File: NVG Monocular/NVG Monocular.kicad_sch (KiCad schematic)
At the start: 13 parts, among them U1 MP2696AGQ-0000-P

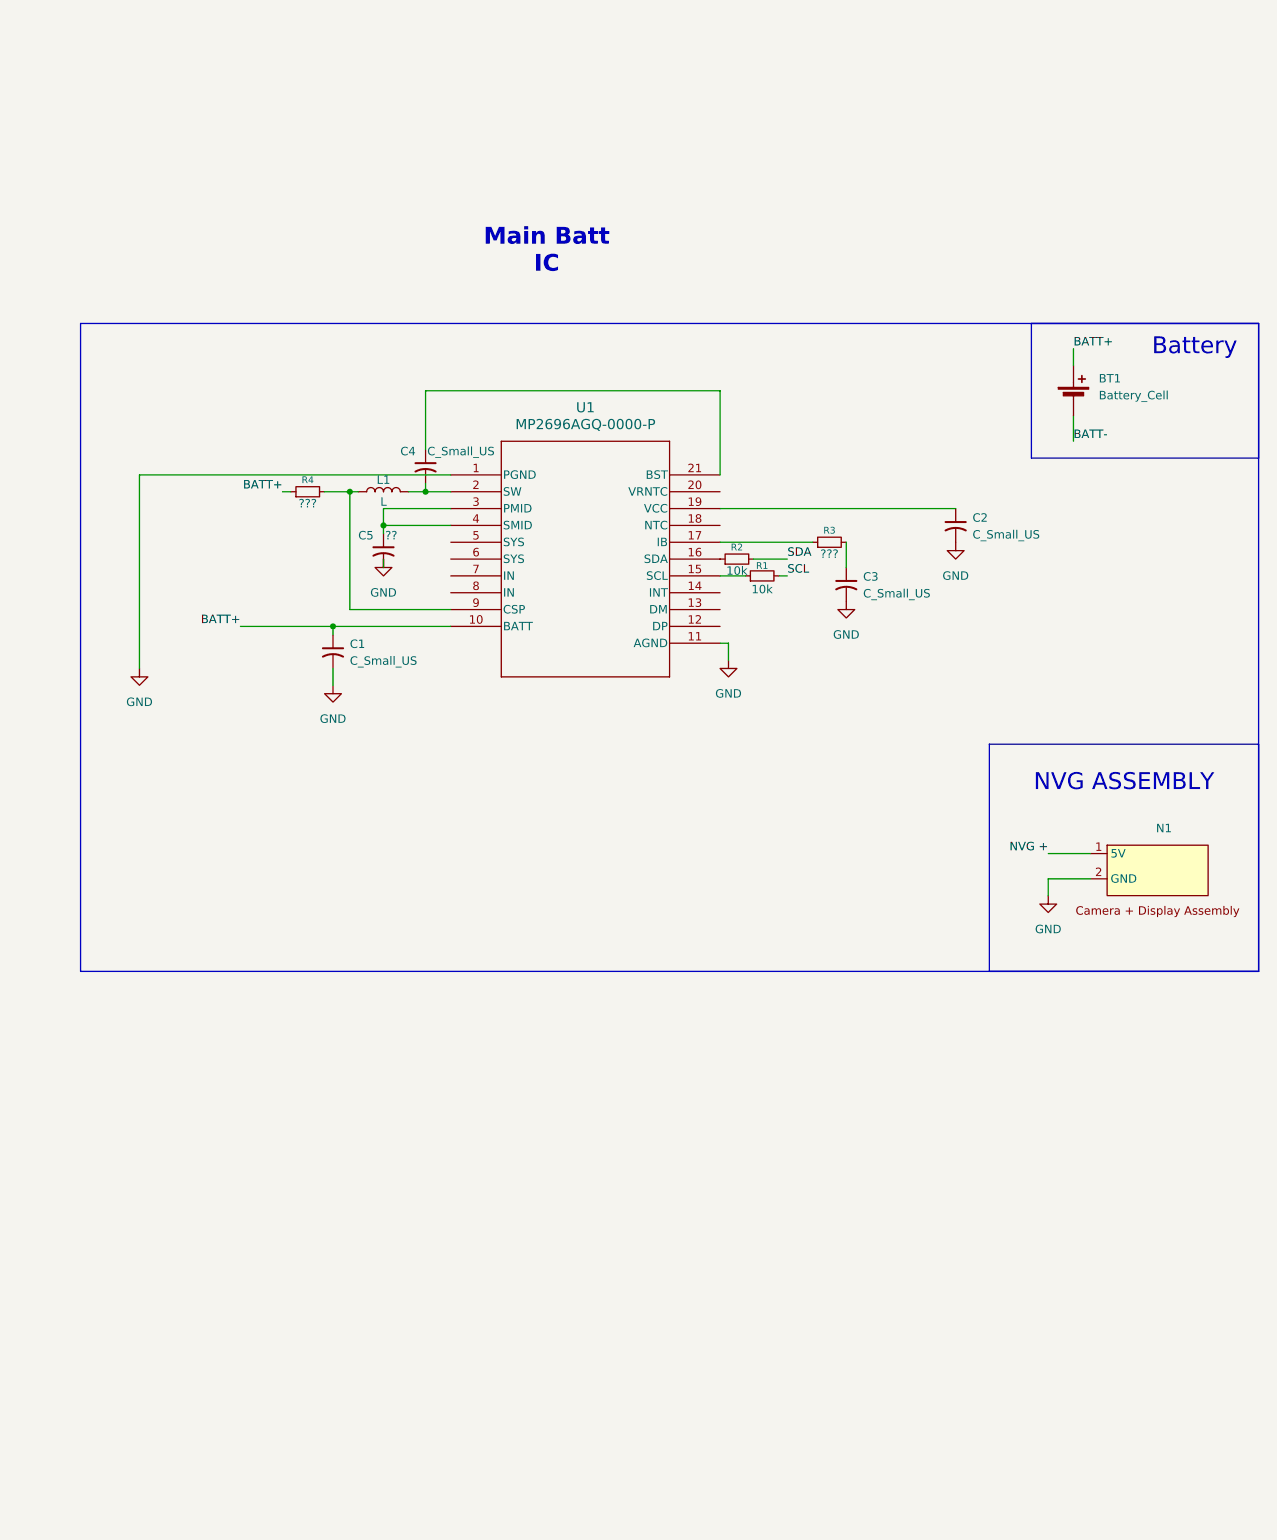
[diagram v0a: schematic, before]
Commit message: Added USB-C and speced out Charge IC passives
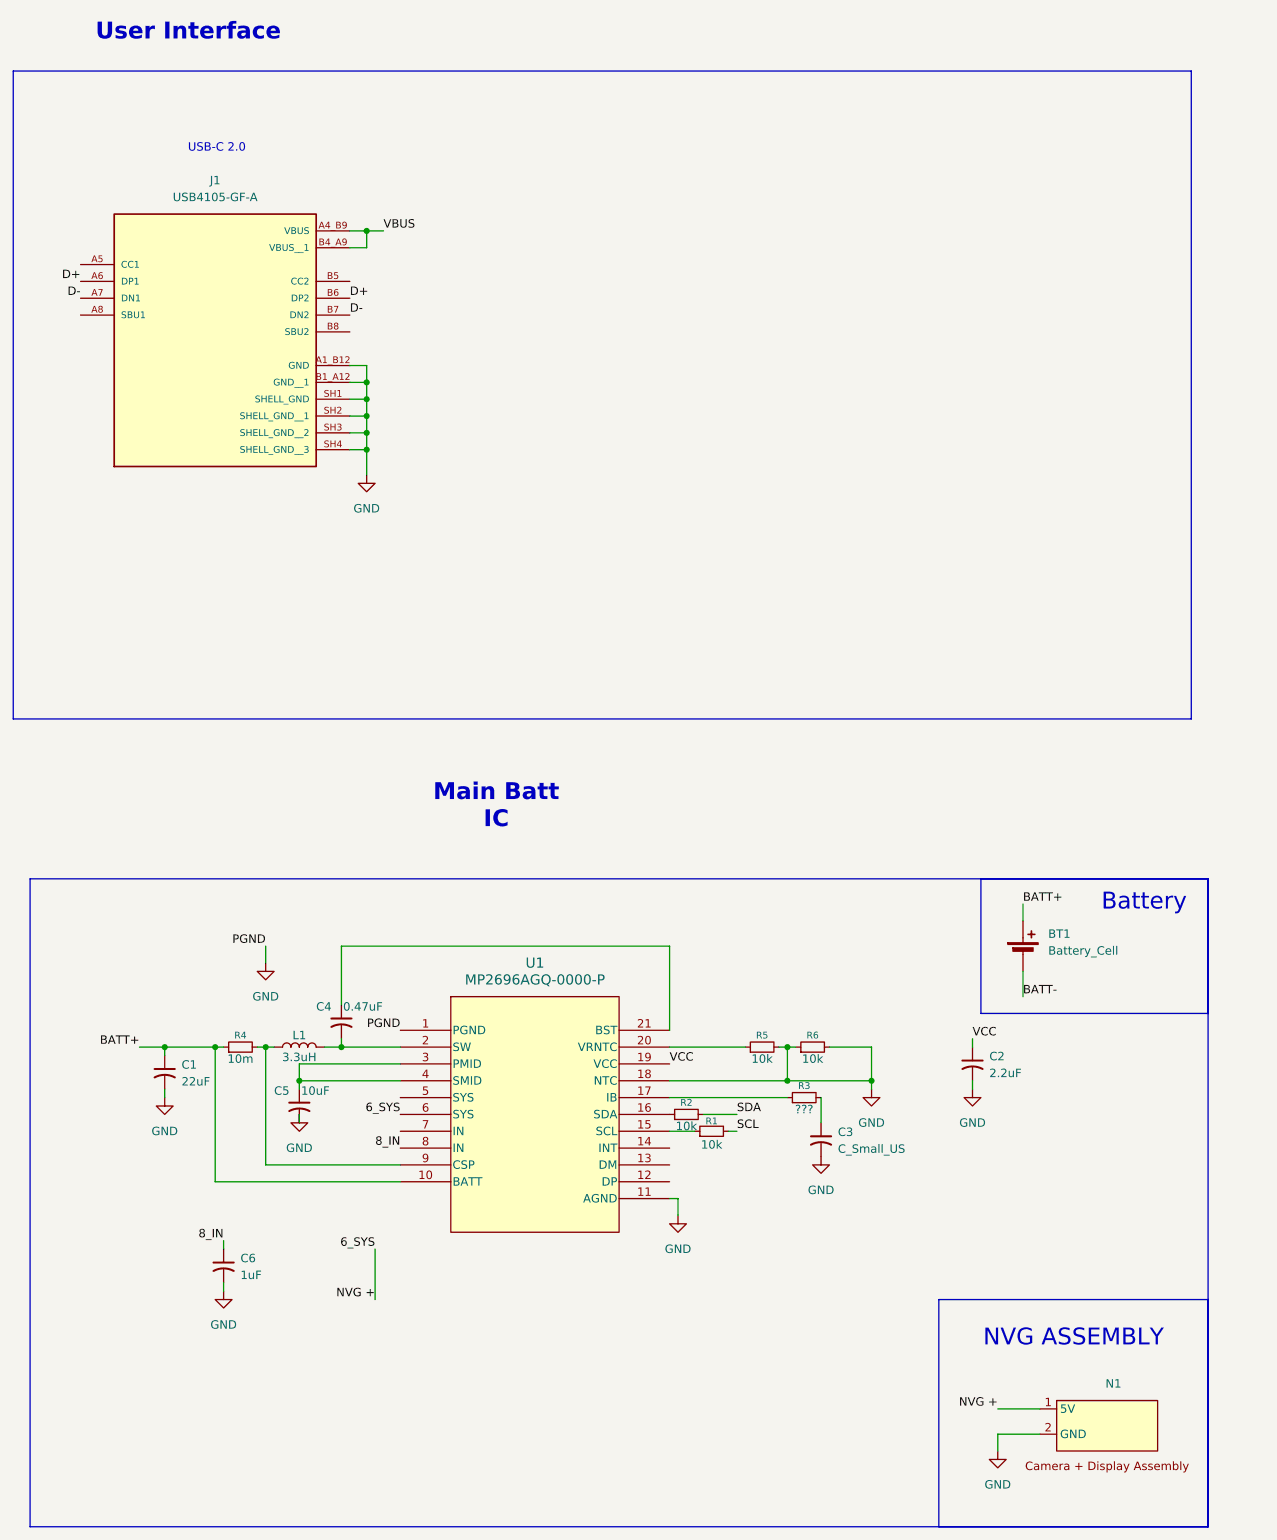
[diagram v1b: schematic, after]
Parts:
- added C6: 1uF, Capacitor_SMD:C_0603_1608Metric_Pad1.08x0.95mm_HandSolder, symbol Device:C_Small_US
- added J1: USB4105-GF-A, USB4105-GF-A:GCT_USB4105-GF-A, symbol USB4105:USB4105-GF-A
- added R5, R6: 10k, Resistor_SMD:R_0603_1608Metric, symbol Device:R_Small
- BT1: now left out of the parts list
- C1: value C_Small_US -> 22uF; footprint (none) -> Capacitor_SMD:C_0603_1608Metric_Pad1.08x0.95mm_HandSolder
- C2: value C_Small_US -> 2.2uF; footprint (none) -> Capacitor_SMD:C_0603_1608Metric_Pad1.08x0.95mm_HandSolder
- C4: value C_Small_US -> 0.47uF; footprint (none) -> Capacitor_SMD:C_0603_1608Metric_Pad1.08x0.95mm_HandSolder
- C5: value ?? -> 10uF; footprint (none) -> Capacitor_SMD:C_0805_2012Metric_Pad1.18x1.45mm_HandSolder
- L1: value L -> 3.3uH; footprint (none) -> IHLM2525CZER3R3M01:IND_IHLM-2525CZ_VIS
- R1, R2: footprint (none) -> Resistor_SMD:R_0603_1608Metric
- R4: value ??? -> 10m; footprint (none) -> Resistor_SMD:R_1206_3216Metric_Pad1.30x1.75mm_HandSolder
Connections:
- net NVG + is gone; now on net 6_SYS: N1.1 (5V)
- net GND: now also U1.18 (NTC), C6.2, J1.A1_B12 (GND), J1.B1_A12 (GND__1), J1.SH1 (SHELL_GND), J1.SH2 (SHELL_GND__1), J1.SH3 (SHELL_GND__2), J1.SH4 (SHELL_GND__3), R5.2, R6.1, R6.2
- net VCC: now reaches C2.1, U1.19 (VCC)
- net at U1.20 (VRNTC): now also R5.1
- net 6_SYS: now reaches U1.6 (SYS)
- net 8_IN: now reaches U1.8 (IN)
- net 8_IN: now also C6.1
- new net D+: J1.A6 (DP1), J1.B6 (DP2)
- new net D-: J1.A7 (DN1), J1.B7 (DN2)
- new net VBUS: J1.A4_B9 (VBUS), J1.B4_A9 (VBUS__1)
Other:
- note added: "USB-C 2.0"
- note added: "User Interface"
- moved on the sheet: BT1, C1, C2, C3, C4, C5, L1, N1, R1, R2, R3, R4

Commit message: Schematic ready for layout
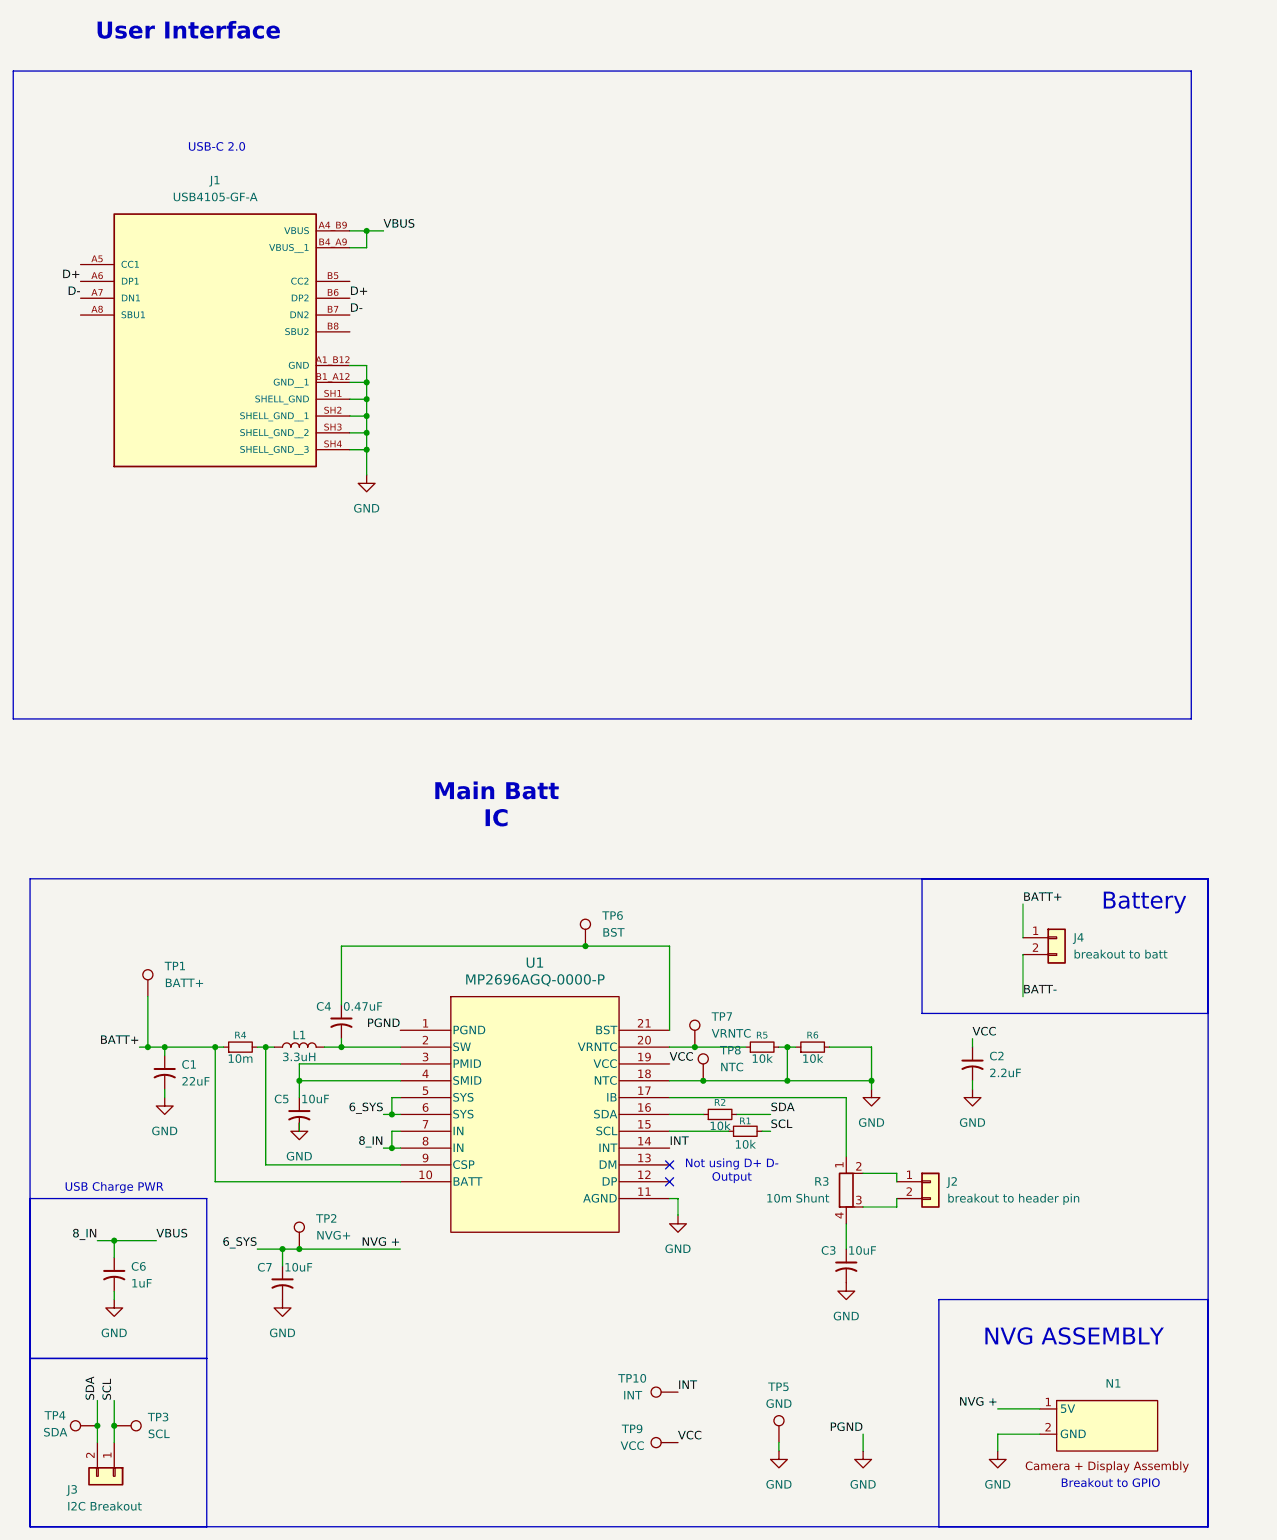
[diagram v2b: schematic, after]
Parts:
- removed BT1: Battery_Cell, symbol Device:Battery_Cell
- removed R3: ???, symbol Device:R_Small
- added C7: 10uF, Capacitor_SMD:C_0805_2012Metric_Pad1.18x1.45mm_HandSolder, symbol Device:C_Small_US
- added J2: breakout to header pin, Connector_PinHeader_1.00mm:PinHeader_1x02_P1.00mm_Vertical, symbol Connector_Generic:Conn_01x02
- added J3: I2C Breakout, symbol Connector_Generic:Conn_01x02
- added J4: breakout to batt, Connector_PinHeader_1.00mm:PinHeader_1x02_P1.00mm_Vertical, symbol Connector_Generic:Conn_01x02
- added R3: 10m Shunt, Resistor_SMD:R_0603_1608Metric_Pad0.98x0.95mm_HandSolder, symbol Device:R_Shunt
- added TP1: BATT+, TestPoint:TestPoint_Pad_D1.5mm, symbol Connector:TestPoint
- added TP10: INT, TestPoint:TestPoint_Pad_D1.5mm, symbol Connector:TestPoint
- added TP2: NVG+, TestPoint:TestPoint_Pad_D1.5mm, symbol Connector:TestPoint
- added TP3: SCL, TestPoint:TestPoint_Pad_D1.5mm, symbol Connector:TestPoint
- added TP4: SDA, TestPoint:TestPoint_Pad_D1.5mm, symbol Connector:TestPoint
- added TP5: GND, TestPoint:TestPoint_Pad_D1.5mm, symbol Connector:TestPoint
- added TP6: BST, TestPoint:TestPoint_Pad_D1.5mm, symbol Connector:TestPoint
- added TP7: VRNTC, TestPoint:TestPoint_Pad_D1.5mm, symbol Connector:TestPoint
- added TP8: NTC, TestPoint:TestPoint_Pad_D1.5mm, symbol Connector:TestPoint
- added TP9: VCC, TestPoint:TestPoint_Pad_D1.5mm, symbol Connector:TestPoint
- C3: value C_Small_US -> 10uF; footprint (none) -> Capacitor_SMD:C_0805_2012Metric_Pad1.18x1.45mm_HandSolder
- N1: footprint (none) -> Connector_PinHeader_1.00mm:PinHeader_1x02_P1.00mm_Vertical
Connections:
- net VBUS is gone; now on net 8_IN: J1.A4_B9 (VBUS), J1.B4_A9 (VBUS__1)
- net 6_SYS: now also U1.5 (SYS), C7.1, TP2.1
- net 8_IN: now also U1.7 (IN)
- net BATT+: now also J4.1 (Pin_1), TP1.1
- net BATT-: now also J4.2 (Pin_2)
- net GND: now also C7.2, TP5.1, TP8.1
- net SCL: now also J3.1 (Pin_1), TP3.1
- net SDA: now also J3.2 (Pin_2), TP4.1
- net VCC: now also TP9.1
- net at U1.17 (IB): now also R3.1
- net at C3.1: now also R3.4
- net at C4.1, U1.21 (BST): now also TP6.1
- net INT: now reaches U1.14 (INT)
- net INT: now also TP10.1
- net at R5.1, U1.20 (VRNTC): now also TP7.1
- new net: J2.1 (Pin_1), R3.2
- new net: J2.2 (Pin_2), R3.3
- no-connect marks 0 -> 2
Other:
- note added: "Breakout to GPIO"
- note added: "Not using D+ D- Output"
- note added: "USB Charge PWR"
- moved on the sheet: C5, C6, R1, R2

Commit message: layout partialy finished, some test points removed
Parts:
- removed TP2: NVG+, TestPoint:TestPoint_Pad_D1.5mm, symbol Connector:TestPoint
- removed TP3: SCL, TestPoint:TestPoint_Pad_D1.5mm, symbol Connector:TestPoint
- removed TP4: SDA, TestPoint:TestPoint_Pad_D1.5mm, symbol Connector:TestPoint
- removed TP8: NTC, TestPoint:TestPoint_Pad_D1.5mm, symbol Connector:TestPoint
- J1: footprint USB4105-GF-A:GCT_USB4105-GF-A -> USB4105:GCT_USB4105-GF-A
- J3: footprint (none) -> Connector_PinHeader_1.00mm:PinHeader_1x02_P1.00mm_Vertical
- R3: symbol Device:R_Shunt -> Device:R
- U1: footprint QFN21_3MMx3MM_MNP -> MP2696AGQ:QFN21_3MMx3MM_MNP
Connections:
- net BATT- is gone; now on net GND: J4.2 (Pin_2)
- net SCL: now also J3.2 (Pin_2); no longer J3.1 (Pin_1)
- net SDA: now also J3.1 (Pin_1); no longer J3.2 (Pin_2)
- net at R3.1, U1.17 (IB): now also J2.1 (Pin_1)
- net at R3.2: now also C3.1, J2.2 (Pin_2); no longer J2.1 (Pin_1)
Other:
- moved on the sheet: C3, J2
